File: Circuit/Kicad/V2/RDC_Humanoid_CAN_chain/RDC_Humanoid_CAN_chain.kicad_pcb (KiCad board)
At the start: 2 copper layers, 69.9 x 25.4 mm, 11 parts, among them J1 R_Root_CAN, J2 L_Root_CAN, J3 CAN_motor1, J4 CAN_motor2, J5 CAN_motor3, J6 CAN_motor6, J7 CAN_motor5, J8 CAN_motor4

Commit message: CANのデイジーチェーン用基板をUpdate
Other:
- board text added: "x"
- board text added: "y"
- board text added: "↓"
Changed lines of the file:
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@@
     (effects (font (size 1 1) (thickness 0.17) bold) (justify left bottom))
+  )
+  (gr_text "↓" (at 83.82 99.06) (layer "F.SilkS")
+    (effects (font (size 6 4) (thickness 0.5)) (justify left bottom))
   )
   (gr_text "R_root" (at 49.92 91.81) (layer "F.SilkS")
@@
     (effects (font (size 1 1) (thickness 0.17) bold) (justify left bottom))
   )
+  (gr_text "↓" (at 91.9988 96.52 90) (layer "F.SilkS")
+    (effects (font (size 6 4) (thickness 0.5)) (justify left bottom))
+  )
   (gr_text "ID:03" (at 60.715 89.27 90) (layer "F.SilkS")
     (effects (font (size 1 1) (thickness 0.17) bold) (justify left bottom))
@@
     (effects (font (size 1 1) (thickness 0.17) bold) (justify left bottom))
   )
+  (gr_text "y" (at 91.44 95.25) (layer "F.SilkS")
+    (effects (font (size 2 2) (thickness 0.2)) (justify left bottom))
+  )
+  (gr_text "x" (at 87.63 99.06) (layer "F.SilkS")
+    (effects (font (size 2 2) (thickness 0.2)) (justify left bottom))
+  )
   (gr_text "ID:00" (at 58.175 77.84 -90) (layer "F.SilkS")

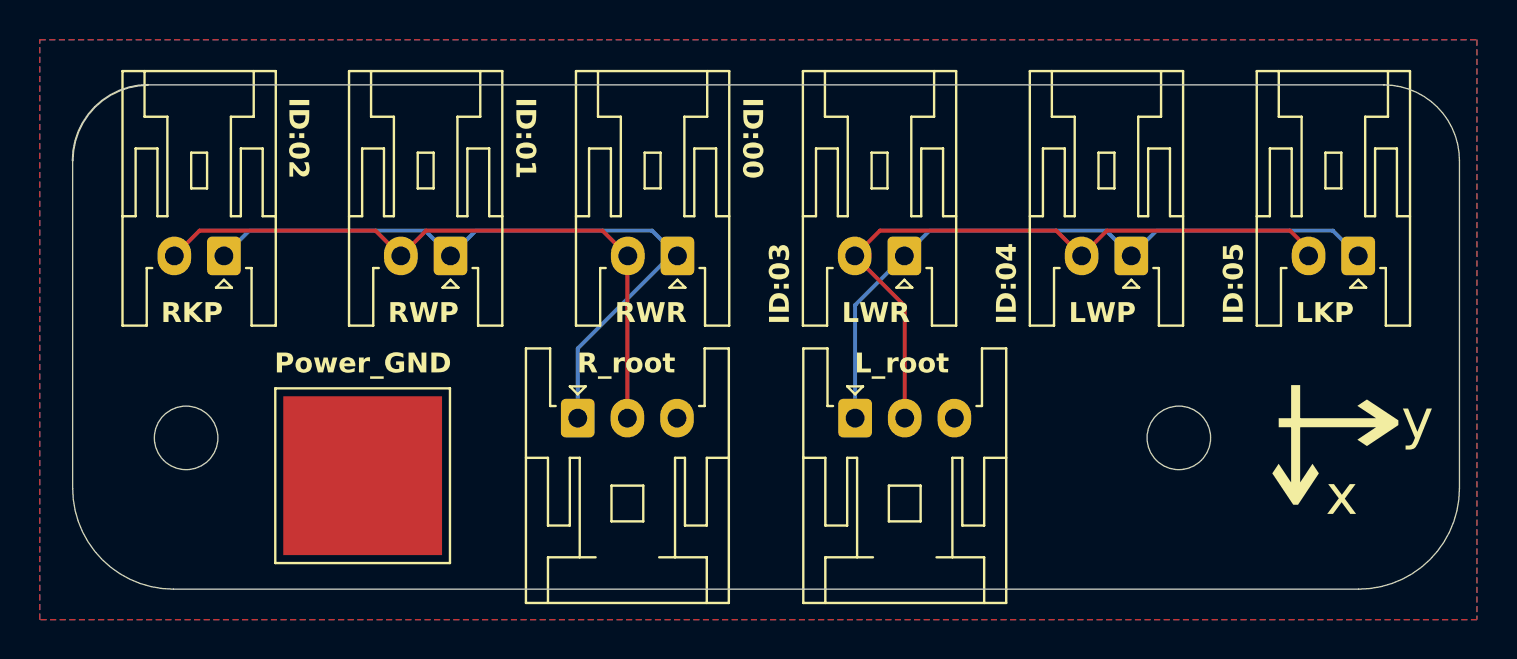
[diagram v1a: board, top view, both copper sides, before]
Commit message: CAN_Chainにビア配置、テキスト整理。Gerberファイル出力
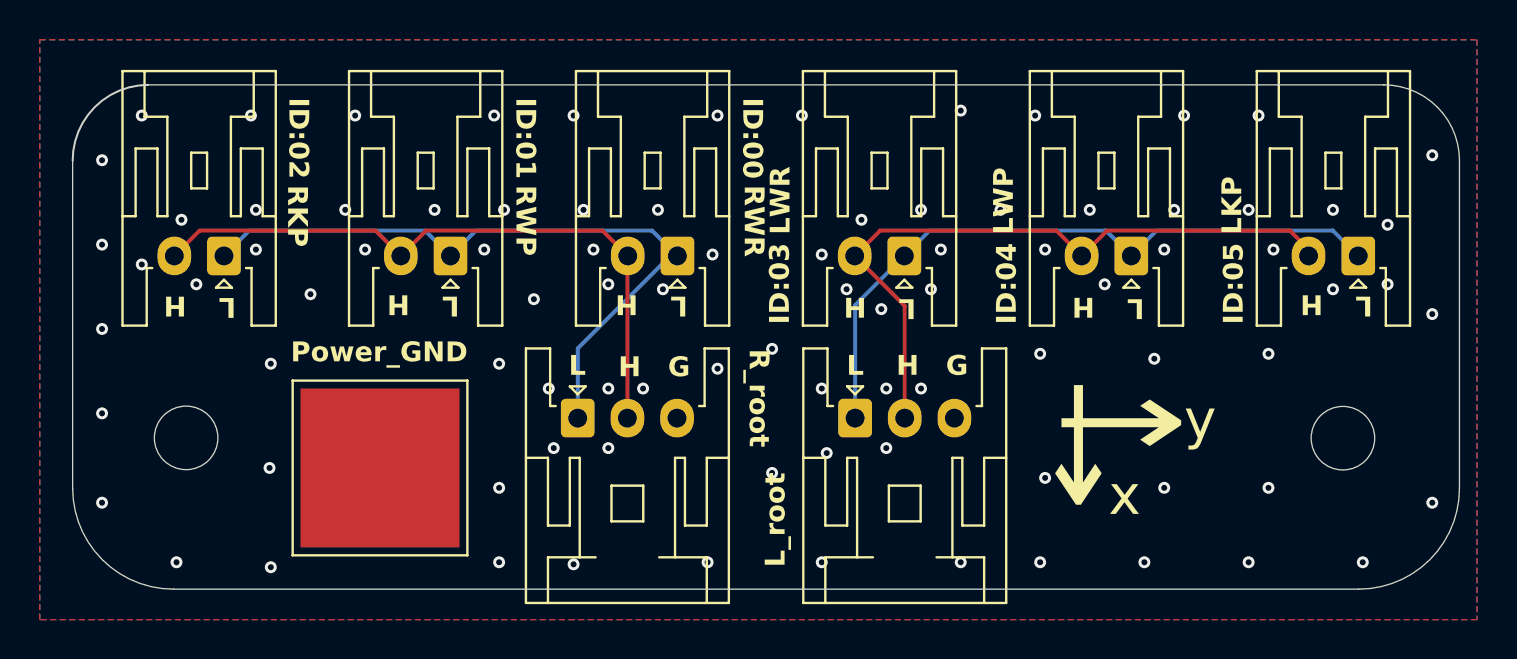
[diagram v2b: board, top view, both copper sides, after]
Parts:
- moved H1 8.27 mm to (88.5, 95.0)
- moved REF** 0.96 mm to (40.0, 96.5)
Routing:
- net GND: vias 0 -> 90
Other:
- board text added: "G"
- board text added: "H"
- board text added: "L"
- board text added: "RDC_Bipedal_Robot - Circuit Name : CAN_Chain - Version : 1.0 - Designed Date : 2025/04/23 - Designer Name - Yusuke Yamasaki"
